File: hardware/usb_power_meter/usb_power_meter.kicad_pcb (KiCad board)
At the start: 4 copper layers, 35.2 x 39.1 mm, 37 parts, among them J1 Conn_ARM_JTAG_SWD_10, J2 USB_A, J4 USB_A, Q1 2N7002, Q2 IRML6401, U1 nRF52833-QDxx, U2 INA226, X1 32Mhz crystal, X2 32.768kHz crystal

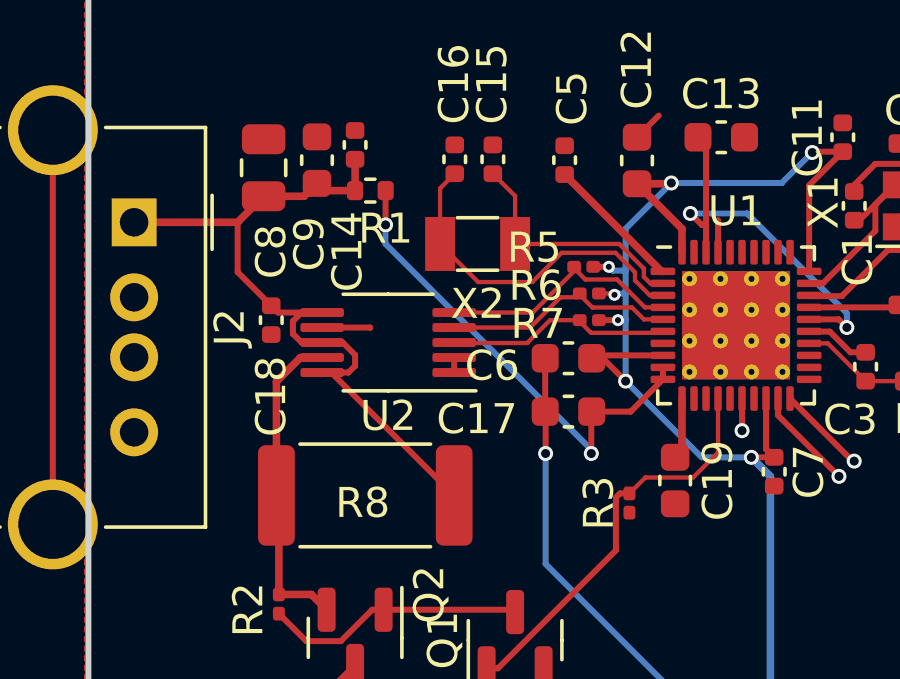
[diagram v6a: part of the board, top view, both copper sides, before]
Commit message: Fix INA226 power supply and use proper 4-wire connection for the shunt resistor
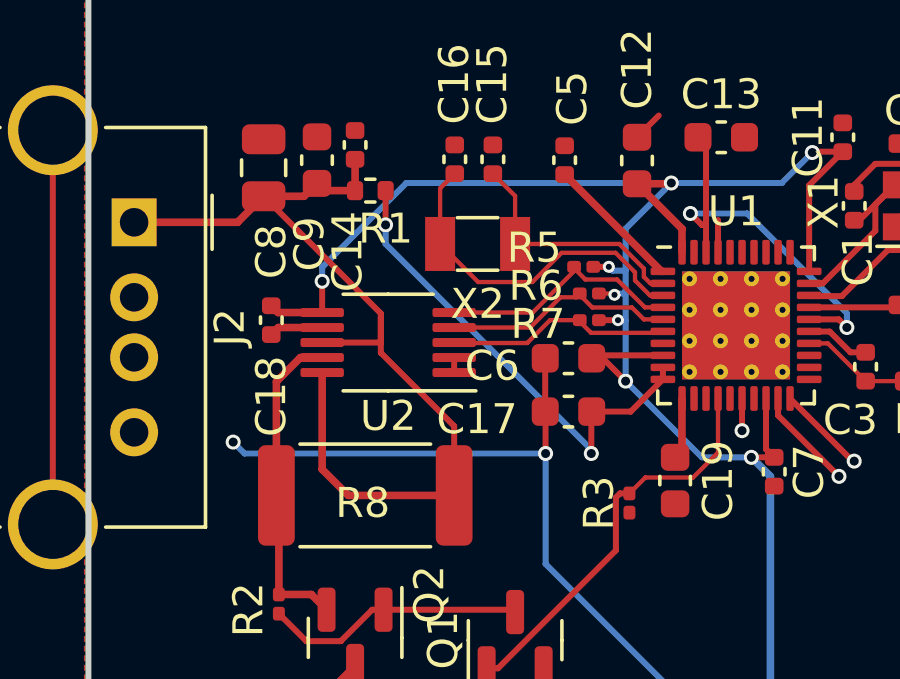
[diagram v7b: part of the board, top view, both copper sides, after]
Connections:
- C18 pad 1: VBUS -> VDD
- U2 pad 6: VBUS -> VDD
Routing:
- net VDD: track 60.1 -> 76.2 mm, vias 8 -> 9
- net GND: track 26.4 -> 37.1 mm, vias 2 -> 3
- net VBUS: track 25.6 -> 33.1 mm
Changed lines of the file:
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@@
       (net 15 "Net-(U1-AIN2{slash}P0.04)") (pinfunction "SCL") (pintype "input"))
     (pad "6" smd roundrect (at 2.2 1 180) (size 1.45 0.3) (layers "F.Cu" "F.Paste" "F.Mask") (roundrect_rratio 0.25)
-      (net 14 "VBUS") (pinfunction "VS") (pintype "power_in"))
+      (net 6 "VDD") (pinfunction "VS") (pintype "power_in"))
     (pad "7" smd roundrect (at 2.2 0.5 180) (size 1.45 0.3) (layers "F.Cu" "F.Paste" "F.Mask") (roundrect_rratio 0.25)
       (net 1 "GND") (pinfunction "GND") (pintype "power_in"))
@@
       (stroke (width 0.1) (type solid)) (layer "F.Fab"))
     (pad "1" smd roundrect (at -0.48 0 270) (size 0.56 0.62) (layers "F.Cu" "F.Paste" "F.Mask") (roundrect_rratio 0.25)
-      (net 14 "VBUS") (pintype "passive"))
+      (net 6 "VDD") (pintype "passive"))
     (pad "2" smd roundrect (at 0.48 0 270) (size 0.56 0.62) (layers "F.Cu" "F.Paste" "F.Mask") (roundrect_rratio 0.25)
       (net 1 "GND") (pintype "passive"))
@@
   (gr_rect (start 112.522 91.186) (end 147.701 130.302)
     (stroke (width 0.2) (type default)) (fill none) (layer "Edge.Cuts"))
+  (segment (start 118.852 102.862) (end 120.314 102.862) (width 0.254) (layer "F.Cu") (net 1))
+  (segment (start 118.618 103.096) (end 118.852 102.862) (width 0.254) (layer "F.Cu") (net 1))
   (segment (start 138.754 97.406) (end 138.049 98.111) (width 0.2) (layer "F.Cu") (net 1))
   (segment (start 140.504 97.456) (end 140.454 97.406) (width 0.2) (layer "F.Cu") (net 1))
@@
   (segment (start 124.714 103.862) (end 124.714 104.362) (width 0.2) (layer "F.Cu") (net 1))
   (segment (start 130.81 96.52) (end 131.535 95.795) (width 0.2) (layer "F.Cu") (net 1))
-  (segment (start 120.314 102.862) (end 121.912 102.862) (width 0.2) (layer "F.Cu") (net 1))
   (segment (start 127.725 103.862) (end 127.749 103.886) (width 0.2) (layer "F.Cu") (net 1))
   (segment (start 131.786 109.032) (end 132.08 108.738) (width 0.2) (layer "F.Cu") (net 1))
@@
   (segment (start 127.749 103.886) (end 127.749 105.664) (width 0.2) (layer "F.Cu") (net 1))
   (segment (start 136.5475 102.99) (end 136.645 102.99) (width 0.2) (layer "F.Cu") (net 1))
-  (segment (start 121.912 102.862) (end 121.92 102.87) (width 0.2) (layer "F.Cu") (net 1))
   (segment (start 139.404 99.356) (end 139.404 99.506) (width 0.2) (layer "F.Cu") (net 1))
   (segment (start 140.504 98.256) (end 139.404 99.356) (width 0.2) (layer "F.Cu") (net 1))
@@
   (via (at 132.08 115.062) (size 0.5) (drill 0.3) (layers "F.Cu" "B.Cu") (free) (net 1))
   (via (at 127.762 107.061) (size 0.5) (drill 0.3) (layers "F.Cu" "B.Cu") (free) (net 1))
+  (via (at 117.348 106.68) (size 0.5) (drill 0.3) (layers "F.Cu" "B.Cu") (free) (net 1))
+  (segment (start 127.762 107.061) (end 117.729 107.061) (width 0.2) (layer "B.Cu") (net 1))
+  (segment (start 117.729 107.061) (end 117.348 106.68) (width 0.2) (layer "B.Cu") (net 1))
   (segment (start 127.762 110.744) (end 127.762 107.061) (width 0.2) (layer "B.Cu") (net 1))
   (segment (start 132.08 115.062) (end 127.762 110.744) (width 0.2) (layer "B.Cu") (net 1))
@@
   (segment (start 129.54 101.727) (end 130.013813 101.727) (width 0.145) (layer "F.Cu") (net 6))
   (segment (start 130.013813 101.727) (end 130.058313 101.7715) (width 0.145) (layer "F.Cu") (net 6))
+  (segment (start 120.314355 102.361645) (end 120.314 102.362) (width 0.2) (layer "F.Cu") (net 6))
   (segment (start 135.382 107.188) (end 134.62 107.188) (width 0.2) (layer "F.Cu") (net 6))
   (segment (start 132.308 99.568) (end 132.308 100.3525) (width 0.254) (layer "F.Cu") (net 6))
+  (segment (start 120.314355 101.3206) (end 120.314355 102.361645) (width 0.2) (layer "F.Cu") (net 6))
   (segment (start 135.382 107.188) (end 135.11 106.916) (width 0.2) (layer "F.Cu") (net 6))
   (segment (start 129.54 102.616) (end 130.175 102.616) (width 0.2) (layer "F.Cu") (net 6))
@@
   (segment (start 129.299 103.886) (end 129.395 103.79) (width 0.2) (layer "F.Cu") (net 6))
   (segment (start 137.668 97) (end 136.68 97) (width 0.2) (layer "F.Cu") (net 6))
+  (segment (start 120.314 102.362) (end 118.844 102.362) (width 0.254) (layer "F.Cu") (net 6))
   (segment (start 136.68 97) (end 136.652 97.028) (width 0.2) (layer "F.Cu") (net 6))
+  (segment (start 118.844 102.362) (end 118.618 102.136) (width 0.254) (layer "F.Cu") (net 6))
   (segment (start 129.299 103.886) (end 129.667 103.886) (width 0.2) (layer "F.Cu") (net 6))
   (segment (start 130.175 126.283) (end 130.048 126.41) (width 0.254) (layer "F.Cu") (net 6))
@@
   (via (at 130.429 104.648) (size 0.5) (drill 0.3) (layers "F.Cu" "B.Cu") (free) (net 6))
   (via (at 136.652 97.028) (size 0.5) (drill 0.3) (layers "F.Cu" "B.Cu") (free) (net 6))
+  (via (at 120.314355 101.3206) (size 0.5) (drill 0.3) (layers "F.Cu" "B.Cu") (net 6))
   (via (at 130.175 102.616) (size 0.4) (drill 0.2) (layers "F.Cu" "B.Cu") (free) (net 6))
   (via (at 129.8702 100.838) (size 0.4) (drill 0.2) (layers "F.Cu" "B.Cu") (free) (net 6))
@@
   (segment (start 130.429 104.648) (end 130.429 102.616) (width 0.2) (layer "B.Cu") (net 6))
   (segment (start 135.636 98.044) (end 136.652 97.028) (width 0.2) (layer "B.Cu") (net 6))
+  (segment (start 123.117893 98.044) (end 131.953 98.044) (width 0.2) (layer "B.Cu") (net 6))
+  (segment (start 120.314355 100.847538) (end 123.117893 98.044) (width 0.2) (layer "B.Cu") (net 6))
   (segment (start 135.255 114.935) (end 135.255 107.823) (width 0.254) (layer "B.Cu") (net 6))
   (segment (start 131.953 98.044) (end 135.636 98.044) (width 0.2) (layer "B.Cu") (net 6))
+  (segment (start 120.314355 101.3206) (end 120.314355 100.847538) (width 0.2) (layer "B.Cu") (net 6))
   (segment (start 130.429 102.616) (end 130.429 101.727) (width 0.2) (layer "B.Cu") (net 6))
   (segment (start 134.62 107.188) (end 132.969 107.188) (width 0.2) (layer "B.Cu") (net 6))
@@
   (segment (start 117.496 99.354) (end 118.364 98.486) (width 0.254) (layer "F.Cu") (net 14))
   (segment (start 120.314 103.362) (end 120.998619 103.362) (width 0.2) (layer "F.Cu") (net 14))
-  (segment (start 120.618 104.362) (end 124.714 108.458) (width 0.2) (layer "F.Cu") (net 14))
-  (segment (start 119.629381 102.362) (end 120.314 102.362) (width 0.2) (layer "F.Cu") (net 14))
-  (segment (start 121.19 104.362) (end 120.314 104.362) (width 0.2) (layer "F.Cu") (net 14))
-  (segment (start 121.412 103.775381) (end 121.412 104.14) (width 0.2) (layer "F.Cu") (net 14))
-  (segment (start 120.314 104.362) (end 120.618 104.362) (width 0.2) (layer "F.Cu") (net 14))
+  (segment (start 122.27 103.362) (end 122.27 102.5144) (width 0.2) (layer "F.Cu") (net 14))
+  (segment (start 122.27 103.7026) (end 122.27 102.5144) (width 0.2) (layer "F.Cu") (net 14))
+  (segment (start 124.714 106.1466) (end 122.27 103.7026) (width 0.2) (layer "F.Cu") (net 14))
+  (segment (start 121.1834 108.458) (end 124.714 108.458) (width 0.254) (layer "F.Cu") (net 14))
   (segment (start 121.412 98.296) (end 121.41 98.298) (width 0.254) (layer "F.Cu") (net 14))
-  (segment (start 119.339 102.652381) (end 119.629381 102.362) (width 0.2) (layer "F.Cu") (net 14))
-  (segment (start 120.314 103.362) (end 119.629381 103.362) (width 0.2) (layer "F.Cu") (net 14))
   (segment (start 119.713 98.486) (end 120.142 98.057) (width 0.254) (layer "F.Cu") (net 14))
   (segment (start 120.383 98.298) (end 120.142 98.057) (width 0.254) (layer "F.Cu") (net 14))
+  (segment (start 122.27 102.392) (end 118.364 98.486) (width 0.2) (layer "F.Cu") (net 14))
   (segment (start 121.412 97.254) (end 121.412 98.296) (width 0.254) (layer "F.Cu") (net 14))
-  (segment (start 117.496 101.014) (end 117.496 99.354) (width 0.2) (layer "F.Cu") (net 14))
-  (segment (start 119.339 103.071619) (end 119.339 102.652381) (width 0.2) (layer "F.Cu") (net 14))
-  (segment (start 120.314 102.362) (end 118.844 102.362) (width 0.2) (layer "F.Cu") (net 14))
-  (segment (start 119.629381 103.362) (end 119.339 103.071619) (width 0.2) (layer "F.Cu") (net 14))
+  (segment (start 120.314 103.362) (end 122.27 103.362) (width 0.2) (layer "F.Cu") (net 14))
   (segment (start 121.41 98.298) (end 120.383 98.298) (width 0.254) (layer "F.Cu") (net 14))
-  (segment (start 120.998619 103.362) (end 121.412 103.775381) (width 0.2) (layer "F.Cu") (net 14))
-  (segment (start 121.412 104.14) (end 121.19 104.362) (width 0.2) (layer "F.Cu") (net 14))
+  (segment (start 120.314 104.362) (end 120.314 107.5886) (width 0.254) (layer "F.Cu") (net 14))
+  (segment (start 122.27 102.5144) (end 122.27 102.392) (width 0.2) (layer "F.Cu") (net 14))
   (segment (start 114.046 99.354) (end 117.496 99.354) (width 0.254) (layer "F.Cu") (net 14))
-  (segment (start 118.618 102.136) (end 117.496 101.014) (width 0.2) (layer "F.Cu") (net 14))
-  (segment (start 118.844 102.362) (end 118.618 102.136) (width 0.2) (layer "F.Cu") (net 14))
+  (segment (start 120.314 107.5886) (end 121.1834 108.458) (width 0.254) (layer "F.Cu") (net 14))
+  (segment (start 124.714 108.458) (end 124.714 106.1466) (width 0.2) (layer "F.Cu") (net 14))
   (segment (start 118.364 98.486) (end 119.713 98.486) (width 0.254) (layer "F.Cu") (net 14))
   (segment (start 130.144112 101.2605) (end 129.088416 101.2605) (width 0.145) (layer "F.Cu") (net 15))

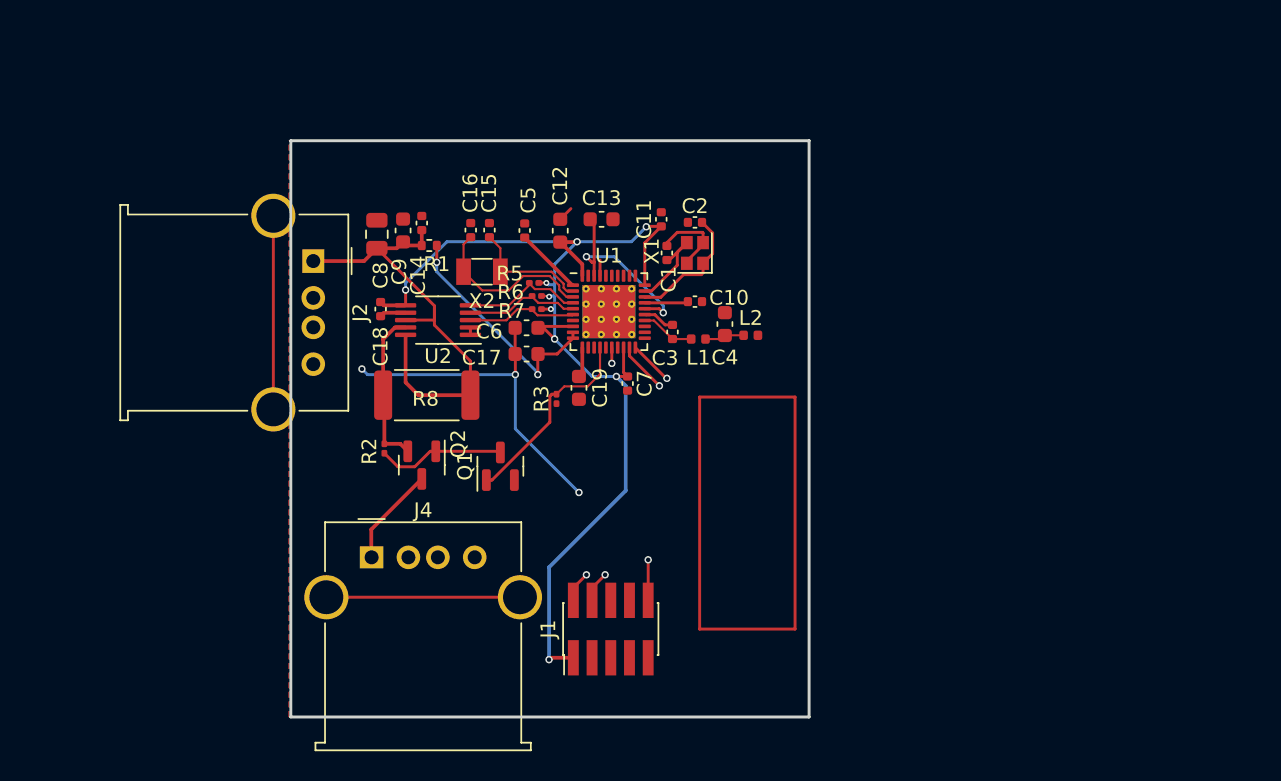
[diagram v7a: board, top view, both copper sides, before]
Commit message: Add an actual USB plug
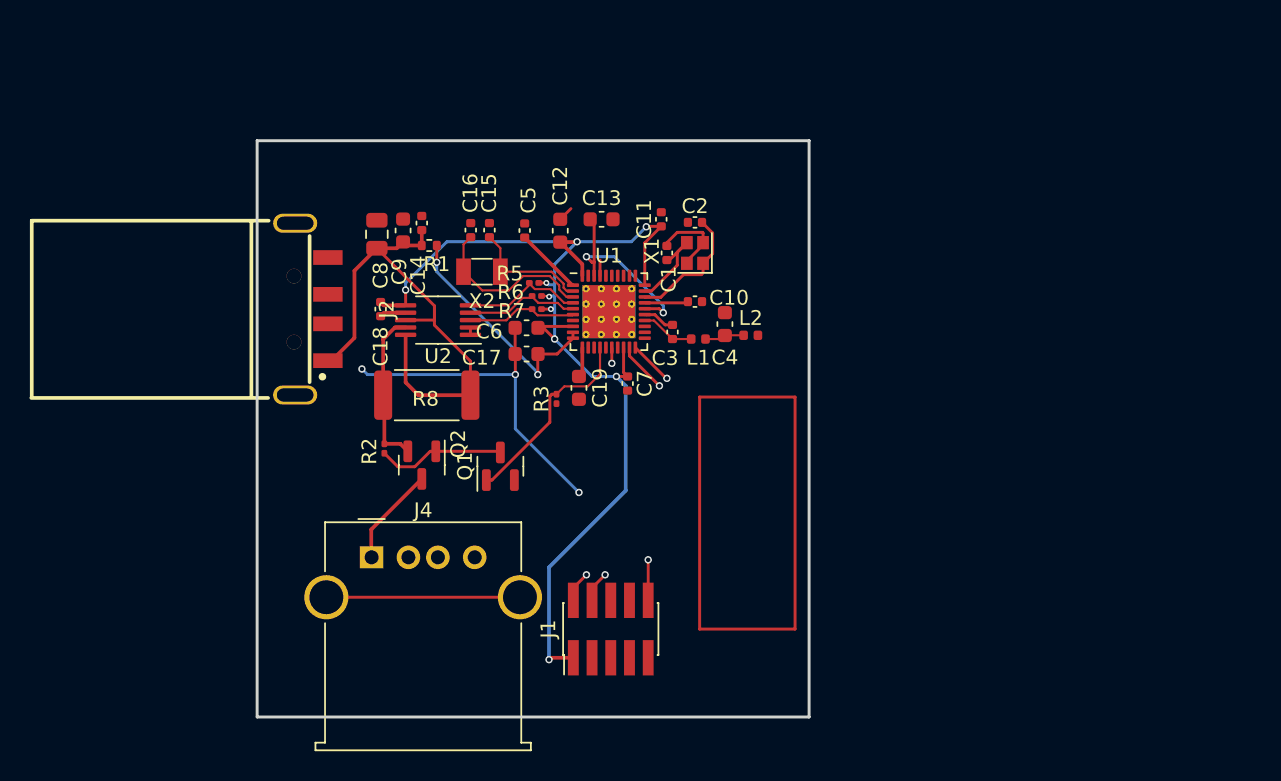
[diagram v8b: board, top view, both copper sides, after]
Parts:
- J2: value USB_A -> 917-P81A202ES60201; footprint Connector_USB:USB_A_Molex_67643_Horizontal -> easyeda2kicad:USB-A-SMD_917-P81A202ES60201
- moved J2 3.26 mm to (113.9, 102.6)
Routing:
- net unconnected-(J2-SHELL-Pad5): track 13.1 -> 0.00 mm
- net VBUS: track 33.1 -> 36.7 mm
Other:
- board size 35.2 x 39.1 mm -> 37.5 x 39.1 mm
